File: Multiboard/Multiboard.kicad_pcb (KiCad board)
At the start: 2 copper layers, 150 x 120 mm, 193 parts, among them J1 Conn_01x20_Socket, J2 Conn_01x20_Socket, J3 Debug, J4 USB_C_Receptacle_USB2.0_16P, J5 Conn_01x06_Socket, J6 Conn_02x20_Odd_Even, J7 Conn_02x20_Odd_Even, J8 USB_C_Receptacle_USB2.0_16P, Q1 Q_Dual_NMOS_G1S2G2D2S1D1, Q2 Q_Dual_NMOS_G1S2G2D2S1D1, Q3 Q_Dual_NMOS_G1S2G2D2S1D1, Q4 Q_Dual_NMOS_G1S2G2D2S1D1, Q5 Q_Dual_NMOS_G1S2G2D2S1D1, Q6 Q_Dual_NMOS_G1S2G2D2S1D1, Q7 Q_Dual_NMOS_G1S2G2D2S1D1, SW1 BOOT0, SW2 NRST, SW3 SW_SPST, SW4 SW_SPST, SW5 SW_SPST, SW6 SW_SPST, SW7 KEY, SW8 SW_SPST, U1 STM32F411RET6, U2 MAX662AESA_T, U3 MCP1792x-3302xCB, U4 FT2232HL-REEL, U5 93LCxxC, U6 LCMXO2-1200ZE-1TG144C, U7 FAN1112, U8 NCP1117, Y1 32.768KHz, Y2 25MHz, Y3 12MHz

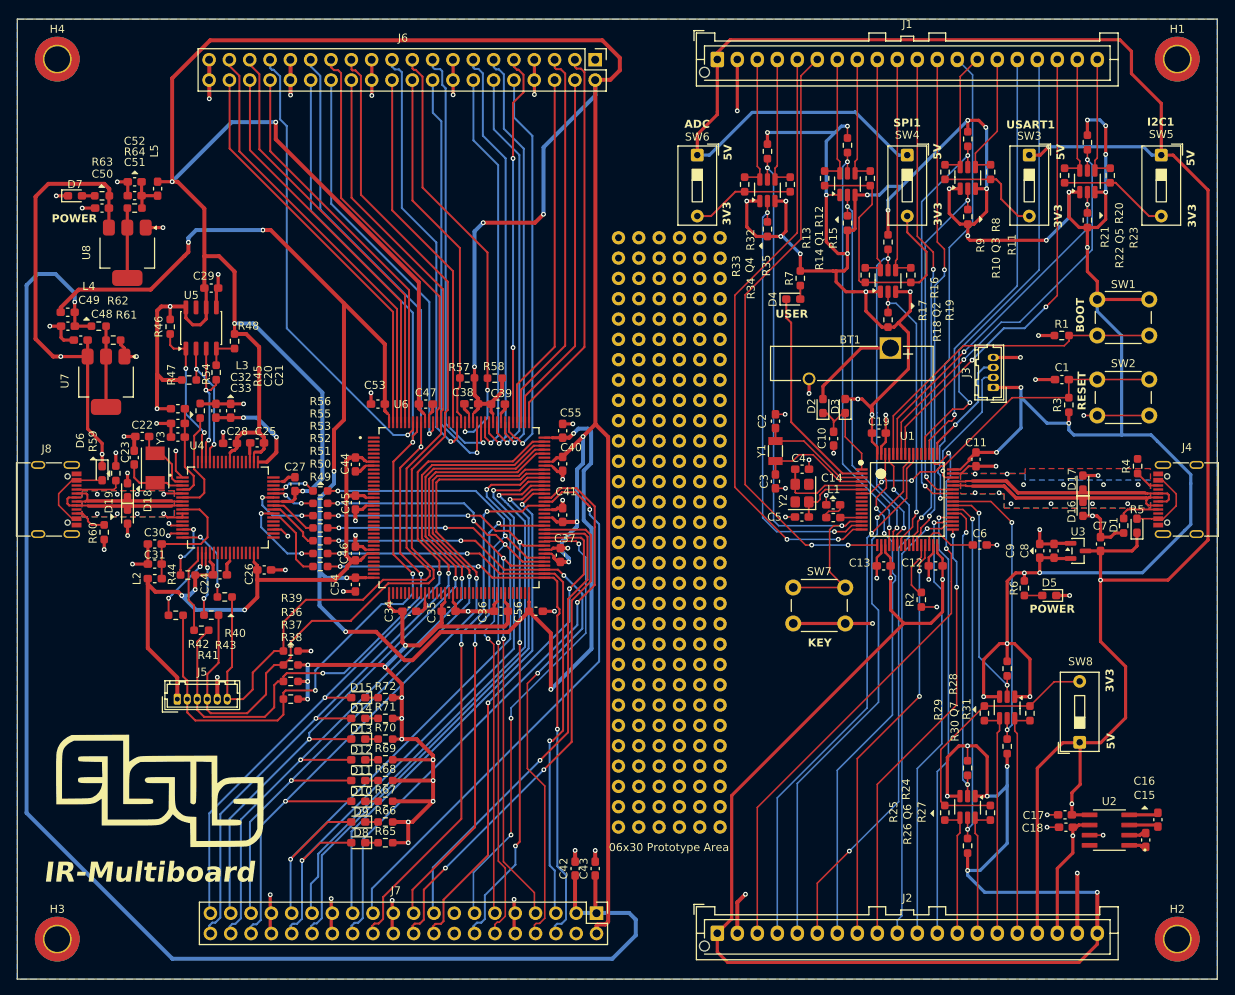
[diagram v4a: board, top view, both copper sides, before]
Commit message: added missing paths
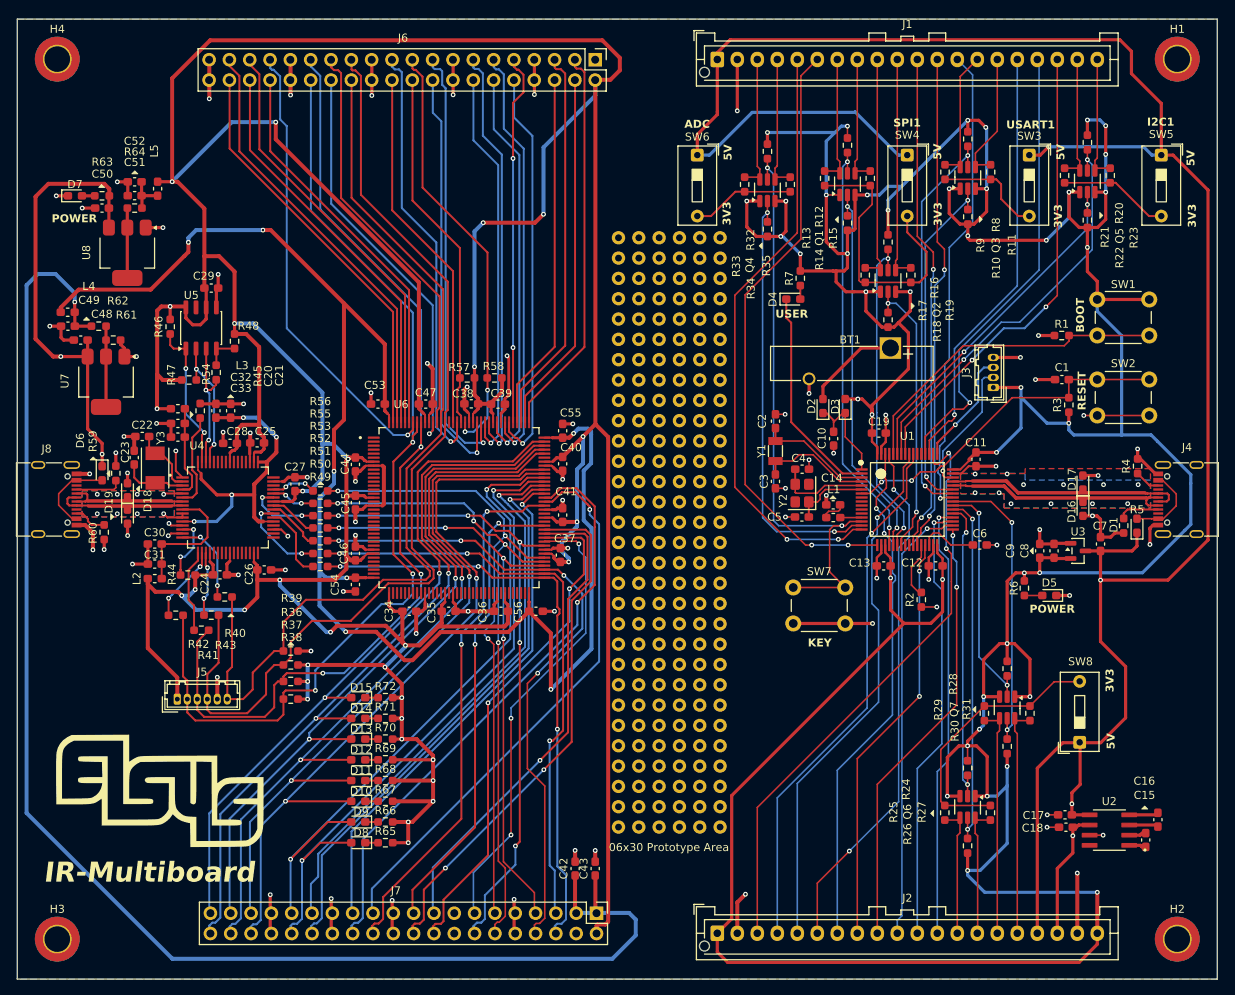
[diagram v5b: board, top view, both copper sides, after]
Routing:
- net GND: track 261.8 -> 305.6 mm, vias 92 -> 104
- net 3V3: track 1200.8 -> 1233.1 mm, vias 70 -> 74
- net 1V8: track 13.2 -> 41.5 mm, vias 2 -> 4
- net Net-(U4-REF): track 13.2 -> 12.0 mm

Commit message: fixed dead copper zones and cleared all errors
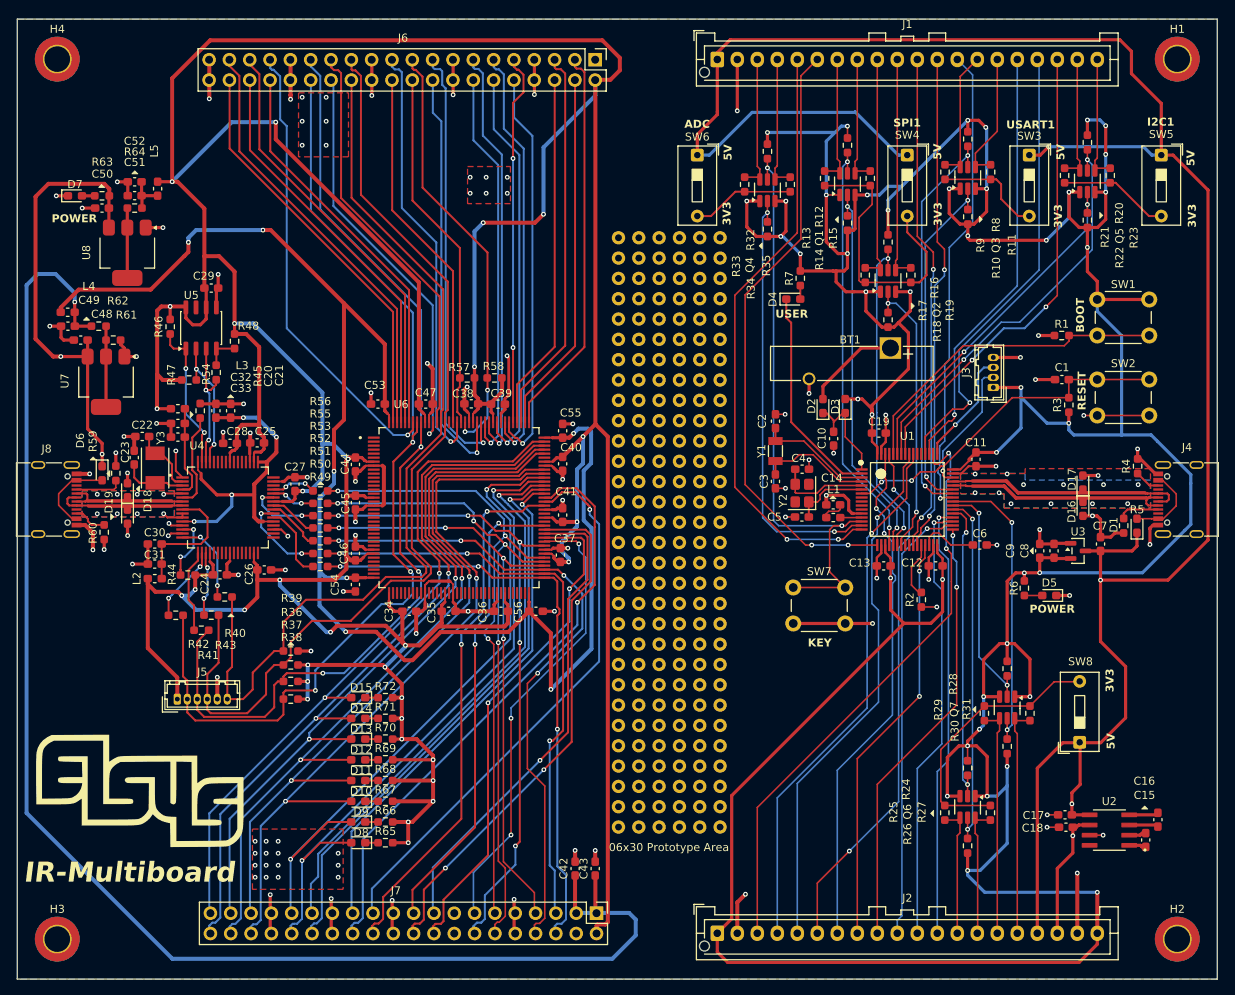
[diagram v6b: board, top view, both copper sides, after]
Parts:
- moved G*** 2.50 mm to (79.8, 134.2)
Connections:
- net 12V renamed 12V_MCU
- net 1V2 renamed 1V2_FPGA
- net 1V8 renamed 1V8_FPGA
- C11 pad 1: 3V3 -> 3V3_MCU
- C12 pad 1: 3V3 -> 3V3_MCU
- C13 pad 1: 3V3 -> 3V3_MCU
- C17 pad 1: 5V -> 5V_MCU
- C19 pad 1: 3V3 -> 3V3_MCU
- C24 pad 1: 3V3 -> 3V3_FPGA
- C25 pad 1: 3V3 -> 3V3_FPGA
- C26 pad 1: 3V3 -> 3V3_FPGA
- C27 pad 1: 3V3 -> 3V3_FPGA
- C28 pad 1: 3V3 -> 3V3_FPGA
- C29 pad 1: 3V3 -> 3V3_FPGA
- C34 pad 1: 3V3 -> 3V3_FPGA
- C35 pad 1: 3V3 -> 3V3_FPGA
- C36 pad 1: 3V3 -> 3V3_FPGA
- C37 pad 1: 3V3 -> 3V3_FPGA
- C38 pad 1: 3V3 -> 3V3_FPGA
- C39 pad 1: 3V3 -> 3V3_FPGA
- C40 pad 1: 3V3 -> 3V3_FPGA
- C41 pad 1: 3V3 -> 3V3_FPGA
- C44 pad 1: 3V3 -> 3V3_FPGA
- C45 pad 1: 3V3 -> 3V3_FPGA
- C46 pad 1: 3V3 -> 3V3_FPGA
- C47 pad 1: 3V3 -> 3V3_FPGA
- C48 pad 1: 5V -> 5V_FPGA
- C50 pad 1: 5V -> 5V_FPGA
- C7 pad 1: 5V -> 5V_MCU
- C8 pad 1: 3V3 -> 3V3_MCU
- C9 pad 1: 3V3 -> 3V3_MCU
- D1 pad 1: 5V -> 5V_MCU
- D3 pad 2: 3V3 -> 3V3_MCU
- D6 pad 1: 5V -> 5V_FPGA
- J1 pad 1: 5V -> 5V_MCU
- J2 pad 1: 3V3 -> 3V3_MCU
- J2 pad 17: 5V -> 5V_MCU
- J2 pad 20: 3V3 -> 3V3_MCU
- J3 pad 1: 3V3 -> 3V3_MCU
- J5 pad 1: 3V3 -> 3V3_FPGA
- J6 pad 2: 3V3 -> 3V3_FPGA
- J7 pad 2: 3V3 -> 3V3_FPGA
- L2 pad 2: 3V3 -> 3V3_FPGA
- L3 pad 2: 3V3 -> 3V3_FPGA
- L5 pad 2: 3V3 -> 3V3_FPGA
- Q1 pad 1: 3V3 -> 3V3_MCU
- Q1 pad 3: 3V3 -> 3V3_MCU
- Q2 pad 1: 3V3 -> 3V3_MCU
- Q2 pad 3: 3V3 -> 3V3_MCU
- Q3 pad 1: 3V3 -> 3V3_MCU
- Q3 pad 3: 3V3 -> 3V3_MCU
- Q4 pad 1: 3V3 -> 3V3_MCU
- Q4 pad 3: 3V3 -> 3V3_MCU
- Q5 pad 1: 3V3 -> 3V3_MCU
- Q5 pad 3: 3V3 -> 3V3_MCU
- Q6 pad 1: 3V3 -> 3V3_MCU
- Q6 pad 3: 3V3 -> 3V3_MCU
- Q7 pad 1: 3V3 -> 3V3_MCU
- Q7 pad 3: 3V3 -> 3V3_MCU
- R10 pad 2: 3V3 -> 3V3_MCU
- R12 pad 2: 3V3 -> 3V3_MCU
- R14 pad 2: 3V3 -> 3V3_MCU
- R16 pad 2: 3V3 -> 3V3_MCU
- R18 pad 2: 3V3 -> 3V3_MCU
- R20 pad 2: 3V3 -> 3V3_MCU
- R22 pad 2: 3V3 -> 3V3_MCU
- R24 pad 2: 3V3 -> 3V3_MCU
- R26 pad 2: 3V3 -> 3V3_MCU
- R28 pad 2: 3V3 -> 3V3_MCU
- R3 pad 1: 3V3 -> 3V3_MCU
- R30 pad 2: 3V3 -> 3V3_MCU
- R32 pad 2: 3V3 -> 3V3_MCU
- R34 pad 2: 3V3 -> 3V3_MCU
- R36 pad 1: 3V3 -> 3V3_FPGA
- R37 pad 1: 3V3 -> 3V3_FPGA
- R38 pad 1: 3V3 -> 3V3_FPGA
- R44 pad 2: 3V3 -> 3V3_FPGA
- R46 pad 2: 3V3 -> 3V3_FPGA
- R47 pad 1: 3V3 -> 3V3_FPGA
- R48 pad 2: 3V3 -> 3V3_FPGA
- R57 pad 1: 3V3 -> 3V3_FPGA
- R58 pad 1: 3V3 -> 3V3_FPGA
- R6 pad 1: 3V3 -> 3V3_MCU
- R63 pad 2: 5V -> 5V_FPGA
- R65 pad 2: 3V3 -> 3V3_FPGA
- R66 pad 2: 3V3 -> 3V3_FPGA
- R67 pad 2: 3V3 -> 3V3_FPGA
- R68 pad 2: 3V3 -> 3V3_FPGA
- R69 pad 2: 3V3 -> 3V3_FPGA
- R7 pad 1: 3V3 -> 3V3_MCU
- R70 pad 2: 3V3 -> 3V3_FPGA
- R71 pad 2: 3V3 -> 3V3_FPGA
- R72 pad 2: 3V3 -> 3V3_FPGA
- R8 pad 2: 3V3 -> 3V3_MCU
- SW1 pad 1: 3V3 -> 3V3_MCU
- SW3 pad 1: 5V -> 5V_MCU
- SW4 pad 1: 5V -> 5V_MCU
- SW5 pad 1: 5V -> 5V_MCU
- SW6 pad 1: 5V -> 5V_MCU
- SW8 pad 1: 5V -> 5V_MCU
- U1 pad 19: 3V3 -> 3V3_MCU
- U1 pad 32: 3V3 -> 3V3_MCU
- U1 pad 48: 3V3 -> 3V3_MCU
- U1 pad 64: 3V3 -> 3V3_MCU
- U2 pad 5: 5V -> 5V_MCU
- U3 pad 2: 3V3 -> 3V3_MCU
- U3 pad 3: 5V -> 5V_MCU
- U4 pad 20: 3V3 -> 3V3_FPGA
- U4 pad 31: 3V3 -> 3V3_FPGA
- U4 pad 42: 3V3 -> 3V3_FPGA
- U4 pad 50: 3V3 -> 3V3_FPGA
- U4 pad 56: 3V3 -> 3V3_FPGA
- U5 pad 6: 3V3 -> 3V3_FPGA
- U5 pad 8: 3V3 -> 3V3_FPGA
- U6 pad 102: 3V3 -> 3V3_FPGA
- U6 pad 118: 3V3 -> 3V3_FPGA
- U6 pad 123: 3V3 -> 3V3_FPGA
- U6 pad 135: 3V3 -> 3V3_FPGA
- U6 pad 16: 3V3 -> 3V3_FPGA
- U6 pad 30: 3V3 -> 3V3_FPGA
- U6 pad 37: 3V3 -> 3V3_FPGA
- U6 pad 51: 3V3 -> 3V3_FPGA
- U6 pad 66: 3V3 -> 3V3_FPGA
- U6 pad 7: 3V3 -> 3V3_FPGA
- U6 pad 79: 3V3 -> 3V3_FPGA
- U6 pad 88: 3V3 -> 3V3_FPGA
- U7 pad 3: 5V -> 5V_FPGA
- U8 pad 3: 5V -> 5V_FPGA
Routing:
- net 3V3: track 1233.1 -> 0.00 mm, vias 74 -> 0
- net 3V3_FPGA: track 0.00 -> 671.4 mm, vias 0 -> 31
- net 3V3_MCU: track 0.00 -> 561.7 mm, vias 0 -> 43
- net 5V: track 329.6 -> 0.00 mm, vias 5 -> 0
- net 5V_MCU: track 0.00 -> 272.8 mm, vias 0 -> 3
- net 5V_FPGA: track 0.00 -> 56.7 mm, vias 0 -> 2
- net GND: track 305.6 -> 318.1 mm, vias 104 -> 131
- net PT11C-TCK: track 117.9 -> 117.0 mm
- net PT11D-TMS: track 123.6 -> 122.8 mm
